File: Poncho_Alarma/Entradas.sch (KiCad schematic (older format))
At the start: 24 parts

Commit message: Esquematico Terminado
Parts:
- added J3: Entradas, symbol Connector_Generic:Conn_01x04
- U1: renamed from U?; symbol EESTN5:TLP627-4 -> Poncho_Alarma-rescue:TLP627-4-EESTN5
- gave numbers to parts that had none: 20
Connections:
- net GND: now also U1.11, U1.13, U1.4, U1.6, U1.8, U1.9; no longer U1.15, U1.15, U1.15, U1.2, U1.2, U1.2
- net at R11.2, R7.2: now also U1.3; no longer U1.1
- net at D6.1 (K), R17.2: now also U1.14, J3.1 (Pin_1); no longer U1.16
- net +3V3: now reaches R16.1, R17.1
- net +3V3: now also R14.1, R15.1, R18.1, R19.1, R20.1, R21.1
- net at R12.2, R8.2: now also U1.5; no longer U1.1
- net at D7.1 (K), R19.2: now also U1.12, J3.2 (Pin_2); no longer U1.16
- net at R13.2, R9.2: now also U1.7; no longer U1.1
- net at D8.1 (K), R21.2: now also U1.10, J3.3 (Pin_3); no longer U1.16
- net at D5.1 (K), R15.2, U1.16: now also J3.4 (Pin_4)
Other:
- moved on the sheet: D5, D8, R10, R13, R14, R15, R20, R21, R6, R9, U1A

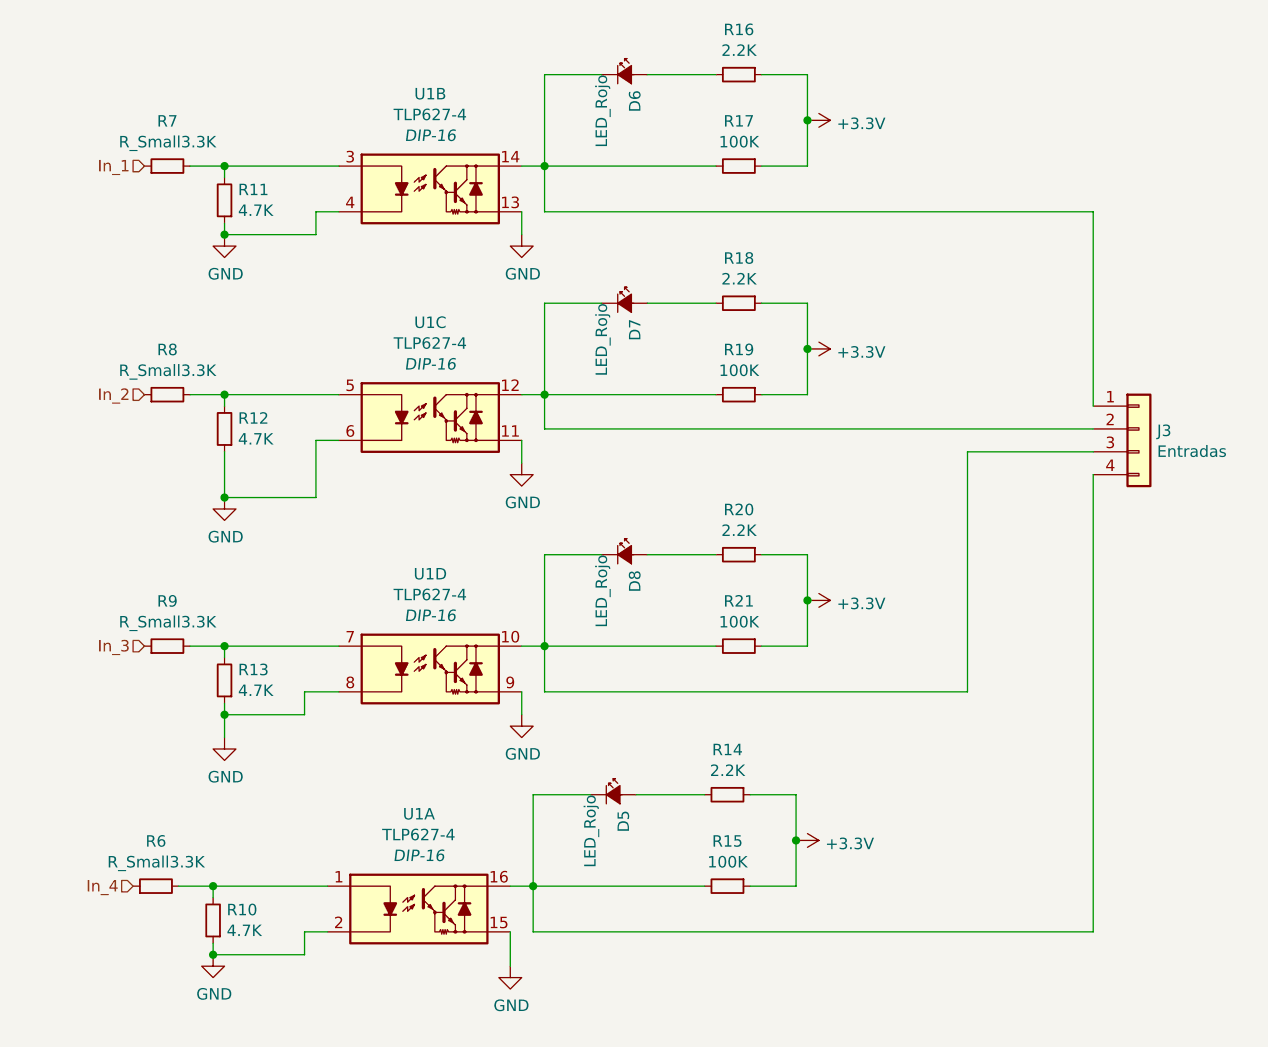
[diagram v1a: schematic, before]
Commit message: asociando componentes
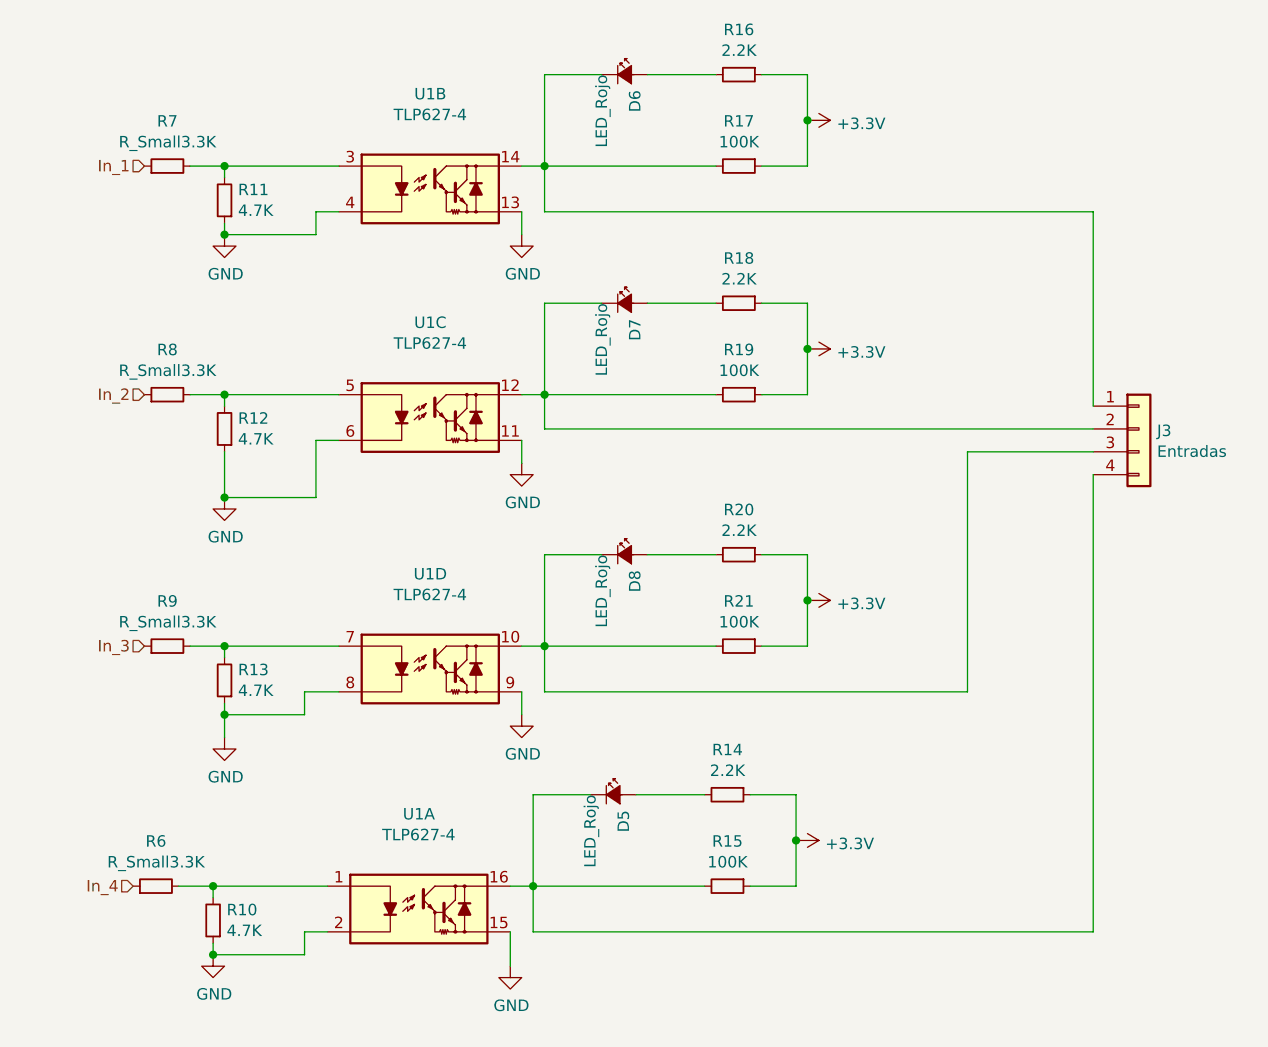
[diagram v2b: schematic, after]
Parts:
- D5, D6, D7, D8: footprint (none) -> LED_SMD:LED_0603_1608Metric_Pad1.05x0.95mm_HandSolder
- J3: footprint (none) -> TerminalBlock:TerminalBlock_bornier-4_P5.08mm
- R10, R11, R12, R13, R14, R15, R16, R17, R18, R19, R20, R21, R6, R7, R8, R9: footprint (none) -> Resistor_SMD:R_0603_1608Metric_Pad1.05x0.95mm_HandSolder
- U1: footprint DIP-16 -> Poncho-PLC:DIP_16-300_socket
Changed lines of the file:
@@
 F 0 "U1" H 4800 2515 50  0000 C CNN
 F 1 "TLP627-4" H 4800 2424 50  0000 C CNN
-F 2 "DIP-16" H 4800 2333 50  0000 C CIN
+F 2 "Poncho-PLC:DIP_16-300_socket" H 4800 2333 50  0001 C CIN
 F 3 "" H 4800 2100 50  0000 L CNN
 	2    4800 2100
@@
 F 0 "D6" V 5696 1532 50  0000 R CNN
 F 1 "LED_Rojo" V 5550 1600 50  0000 R CNN
-F 2 "" V 5650 1600 50  0001 C CNN
+F 2 "LED_SMD:LED_0603_1608Metric_Pad1.05x0.95mm_HandSolder" V 5650 1600 50  0001 C CNN
 F 3 "~" V 5650 1600 50  0001 C CNN
 	1    5650 1600
@@
 F 0 "R16" V 5954 1600 50  0000 C CNN
 F 1 "2.2K" V 6045 1600 50  0000 C CNN
-F 2 "" H 6150 1600 50  0001 C CNN
+F 2 "Resistor_SMD:R_0603_1608Metric_Pad1.05x0.95mm_HandSolder" H 6150 1600 50  0001 C CNN
 F 3 "~" H 6150 1600 50  0001 C CNN
 	1    6150 1600
@@
 F 0 "R17" V 5954 2000 50  0000 C CNN
 F 1 "100K" V 6045 2000 50  0000 C CNN
-F 2 "" H 6150 2000 50  0001 C CNN
+F 2 "Resistor_SMD:R_0603_1608Metric_Pad1.05x0.95mm_HandSolder" H 6150 2000 50  0001 C CNN
 F 3 "~" H 6150 2000 50  0001 C CNN
 	1    6150 2000
@@
 F 0 "R7" V 3846 2000 50  0000 C CNN
 F 1 "R_Small3.3K" V 3755 2000 50  0000 C CNN
-F 2 "" H 3650 2000 50  0001 C CNN
+F 2 "Resistor_SMD:R_0603_1608Metric_Pad1.05x0.95mm_HandSolder" H 3650 2000 50  0001 C CNN
 F 3 "~" H 3650 2000 50  0001 C CNN
 	1    3650 2000
@@
 F 0 "R11" H 3841 2104 50  0000 R CNN
 F 1 "4.7K" H 3841 2195 50  0000 R CNN
-F 2 "" H 3900 2150 50  0001 C CNN
+F 2 "Resistor_SMD:R_0603_1608Metric_Pad1.05x0.95mm_HandSolder" H 3900 2150 50  0001 C CNN
 F 3 "~" H 3900 2150 50  0001 C CNN
 	1    3900 2150
@@
 F 0 "U1" H 4800 3515 50  0000 C CNN
 F 1 "TLP627-4" H 4800 3424 50  0000 C CNN
-F 2 "DIP-16" H 4800 3333 50  0000 C CIN
+F 2 "Poncho-PLC:DIP_16-300_socket" H 4800 3333 50  0001 C CIN
 F 3 "" H 4800 3100 50  0000 L CNN
 	3    4800 3100
@@
 F 0 "D7" V 5696 2532 50  0000 R CNN
 F 1 "LED_Rojo" V 5550 2600 50  0000 R CNN
-F 2 "" V 5650 2600 50  0001 C CNN
+F 2 "LED_SMD:LED_0603_1608Metric_Pad1.05x0.95mm_HandSolder" V 5650 2600 50  0001 C CNN
 F 3 "~" V 5650 2600 50  0001 C CNN
 	1    5650 2600
@@
 F 0 "R18" V 5954 2600 50  0000 C CNN
 F 1 "2.2K" V 6045 2600 50  0000 C CNN
-F 2 "" H 6150 2600 50  0001 C CNN
+F 2 "Resistor_SMD:R_0603_1608Metric_Pad1.05x0.95mm_HandSolder" H 6150 2600 50  0001 C CNN
 F 3 "~" H 6150 2600 50  0001 C CNN
 	1    6150 2600
@@
 F 0 "R19" V 5954 3000 50  0000 C CNN
 F 1 "100K" V 6045 3000 50  0000 C CNN
-F 2 "" H 6150 3000 50  0001 C CNN
+F 2 "Resistor_SMD:R_0603_1608Metric_Pad1.05x0.95mm_HandSolder" H 6150 3000 50  0001 C CNN
 F 3 "~" H 6150 3000 50  0001 C CNN
 	1    6150 3000
@@
 F 0 "R8" V 3846 3000 50  0000 C CNN
 F 1 "R_Small3.3K" V 3755 3000 50  0000 C CNN
-F 2 "" H 3650 3000 50  0001 C CNN
+F 2 "Resistor_SMD:R_0603_1608Metric_Pad1.05x0.95mm_HandSolder" H 3650 3000 50  0001 C CNN
 F 3 "~" H 3650 3000 50  0001 C CNN
 	1    3650 3000
@@
 F 0 "R12" H 3841 3104 50  0000 R CNN
 F 1 "4.7K" H 3841 3195 50  0000 R CNN
-F 2 "" H 3900 3150 50  0001 C CNN
+F 2 "Resistor_SMD:R_0603_1608Metric_Pad1.05x0.95mm_HandSolder" H 3900 3150 50  0001 C CNN
 F 3 "~" H 3900 3150 50  0001 C CNN
 	1    3900 3150
@@
 F 0 "U1" H 4800 4615 50  0000 C CNN
 F 1 "TLP627-4" H 4800 4524 50  0000 C CNN
-F 2 "DIP-16" H 4800 4433 50  0000 C CIN
+F 2 "Poncho-PLC:DIP_16-300_socket" H 4800 4433 50  0001 C CIN
 F 3 "" H 4800 4200 50  0000 L CNN
 	4    4800 4200
@@
 F 0 "D8" V 5696 3632 50  0000 R CNN
 F 1 "LED_Rojo" V 5550 3700 50  0000 R CNN
-F 2 "" V 5650 3700 50  0001 C CNN
+F 2 "LED_SMD:LED_0603_1608Metric_Pad1.05x0.95mm_HandSolder" V 5650 3700 50  0001 C CNN
 F 3 "~" V 5650 3700 50  0001 C CNN
 	1    5650 3700
@@
 F 0 "R20" V 5954 3700 50  0000 C CNN
 F 1 "2.2K" V 6045 3700 50  0000 C CNN
-F 2 "" H 6150 3700 50  0001 C CNN
+F 2 "Resistor_SMD:R_0603_1608Metric_Pad1.05x0.95mm_HandSolder" H 6150 3700 50  0001 C CNN
 F 3 "~" H 6150 3700 50  0001 C CNN
 	1    6150 3700
@@
 F 0 "R21" V 5954 4100 50  0000 C CNN
 F 1 "100K" V 6045 4100 50  0000 C CNN
-F 2 "" H 6150 4100 50  0001 C CNN
+F 2 "Resistor_SMD:R_0603_1608Metric_Pad1.05x0.95mm_HandSolder" H 6150 4100 50  0001 C CNN
 F 3 "~" H 6150 4100 50  0001 C CNN
 	1    6150 4100
@@
 F 0 "R9" V 3846 4100 50  0000 C CNN
 F 1 "R_Small3.3K" V 3755 4100 50  0000 C CNN
-F 2 "" H 3650 4100 50  0001 C CNN
+F 2 "Resistor_SMD:R_0603_1608Metric_Pad1.05x0.95mm_HandSolder" H 3650 4100 50  0001 C CNN
 F 3 "~" H 3650 4100 50  0001 C CNN
 	1    3650 4100
@@
 F 0 "R13" H 3841 4204 50  0000 R CNN
 F 1 "4.7K" H 3841 4295 50  0000 R CNN
-F 2 "" H 3900 4250 50  0001 C CNN
+F 2 "Resistor_SMD:R_0603_1608Metric_Pad1.05x0.95mm_HandSolder" H 3900 4250 50  0001 C CNN
 F 3 "~" H 3900 4250 50  0001 C CNN
 	1    3900 4250
@@
 F 0 "U1" H 4750 5665 50  0000 C CNN
 F 1 "TLP627-4" H 4750 5574 50  0000 C CNN
-F 2 "DIP-16" H 4750 5483 50  0000 C CIN
+F 2 "Poncho-PLC:DIP_16-300_socket" H 4750 5483 50  0001 C CIN
 F 3 "" H 4750 5250 50  0000 L CNN
 	1    4750 5250
@@
 F 0 "D5" V 5646 4682 50  0000 R CNN
 F 1 "LED_Rojo" V 5500 4750 50  0000 R CNN
-F 2 "" V 5600 4750 50  0001 C CNN
+F 2 "LED_SMD:LED_0603_1608Metric_Pad1.05x0.95mm_HandSolder" V 5600 4750 50  0001 C CNN
 F 3 "~" V 5600 4750 50  0001 C CNN
 	1    5600 4750
@@
 F 0 "R14" V 5904 4750 50  0000 C CNN
 F 1 "2.2K" V 5995 4750 50  0000 C CNN
-F 2 "" H 6100 4750 50  0001 C CNN
+F 2 "Resistor_SMD:R_0603_1608Metric_Pad1.05x0.95mm_HandSolder" H 6100 4750 50  0001 C CNN
 F 3 "~" H 6100 4750 50  0001 C CNN
 	1    6100 4750
@@
 F 0 "R15" V 5904 5150 50  0000 C CNN
 F 1 "100K" V 5995 5150 50  0000 C CNN
-F 2 "" H 6100 5150 50  0001 C CNN
+F 2 "Resistor_SMD:R_0603_1608Metric_Pad1.05x0.95mm_HandSolder" H 6100 5150 50  0001 C CNN
 F 3 "~" H 6100 5150 50  0001 C CNN
 	1    6100 5150
@@
 F 0 "R6" V 3796 5150 50  0000 C CNN
 F 1 "R_Small3.3K" V 3705 5150 50  0000 C CNN
-F 2 "" H 3600 5150 50  0001 C CNN
+F 2 "Resistor_SMD:R_0603_1608Metric_Pad1.05x0.95mm_HandSolder" H 3600 5150 50  0001 C CNN
 F 3 "~" H 3600 5150 50  0001 C CNN
 	1    3600 5150
@@
 F 0 "R10" H 3791 5254 50  0000 R CNN
 F 1 "4.7K" H 3791 5345 50  0000 R CNN
-F 2 "" H 3850 5300 50  0001 C CNN
+F 2 "Resistor_SMD:R_0603_1608Metric_Pad1.05x0.95mm_HandSolder" H 3850 5300 50  0001 C CNN
 F 3 "~" H 3850 5300 50  0001 C CNN
 	1    3850 5300
@@
 F 0 "J3" H 7979 3142 50  0000 L CNN
 F 1 "Entradas" H 7979 3051 50  0000 L CNN
-F 2 "" H 7900 3150 50  0001 C CNN
+F 2 "TerminalBlock:TerminalBlock_bornier-4_P5.08mm" H 7900 3150 50  0001 C CNN
 F 3 "~" H 7900 3150 50  0001 C CNN
 	1    7900 3150

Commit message: arreglado lo de la libreria
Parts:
- D5, D6, D7, D8: footprint LED_SMD:LED_0603_1608Metric_Pad1.05x0.95mm_HandSolder -> LED_THT:LED_D3.0mm
- R10, R11, R12, R13, R14, R15, R16, R17, R18, R19, R20, R21, R6, R7, R8, R9: footprint Resistor_SMD:R_0603_1608Metric_Pad1.05x0.95mm_HandSolder -> Resistor_THT:R_Axial_DIN0204_L3.6mm_D1.6mm_P5.08mm_Horizontal
- U1: footprint Poncho-PLC:DIP_16-300_socket -> Package_DIP:DIP-16_W7.62mm
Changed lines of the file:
@@
 F 0 "U1" H 4800 2515 50  0000 C CNN
 F 1 "TLP627-4" H 4800 2424 50  0000 C CNN
-F 2 "Poncho-PLC:DIP_16-300_socket" H 4800 2333 50  0001 C CIN
+F 2 "Package_DIP:DIP-16_W7.62mm" H 4800 2333 50  0001 C CIN
 F 3 "" H 4800 2100 50  0000 L CNN
 	2    4800 2100
@@
 F 0 "D6" V 5696 1532 50  0000 R CNN
 F 1 "LED_Rojo" V 5550 1600 50  0000 R CNN
-F 2 "LED_SMD:LED_0603_1608Metric_Pad1.05x0.95mm_HandSolder" V 5650 1600 50  0001 C CNN
+F 2 "LED_THT:LED_D3.0mm" V 5650 1600 50  0001 C CNN
 F 3 "~" V 5650 1600 50  0001 C CNN
 	1    5650 1600
@@
 F 0 "R16" V 5954 1600 50  0000 C CNN
 F 1 "2.2K" V 6045 1600 50  0000 C CNN
-F 2 "Resistor_SMD:R_0603_1608Metric_Pad1.05x0.95mm_HandSolder" H 6150 1600 50  0001 C CNN
+F 2 "Resistor_THT:R_Axial_DIN0204_L3.6mm_D1.6mm_P5.08mm_Horizontal" H 6150 1600 50  0001 C CNN
 F 3 "~" H 6150 1600 50  0001 C CNN
 	1    6150 1600
@@
 F 0 "R17" V 5954 2000 50  0000 C CNN
 F 1 "100K" V 6045 2000 50  0000 C CNN
-F 2 "Resistor_SMD:R_0603_1608Metric_Pad1.05x0.95mm_HandSolder" H 6150 2000 50  0001 C CNN
+F 2 "Resistor_THT:R_Axial_DIN0204_L3.6mm_D1.6mm_P5.08mm_Horizontal" H 6150 2000 50  0001 C CNN
 F 3 "~" H 6150 2000 50  0001 C CNN
 	1    6150 2000
@@
 F 0 "R7" V 3846 2000 50  0000 C CNN
 F 1 "R_Small3.3K" V 3755 2000 50  0000 C CNN
-F 2 "Resistor_SMD:R_0603_1608Metric_Pad1.05x0.95mm_HandSolder" H 3650 2000 50  0001 C CNN
+F 2 "Resistor_THT:R_Axial_DIN0204_L3.6mm_D1.6mm_P5.08mm_Horizontal" H 3650 2000 50  0001 C CNN
 F 3 "~" H 3650 2000 50  0001 C CNN
 	1    3650 2000
@@
 F 0 "R11" H 3841 2104 50  0000 R CNN
 F 1 "4.7K" H 3841 2195 50  0000 R CNN
-F 2 "Resistor_SMD:R_0603_1608Metric_Pad1.05x0.95mm_HandSolder" H 3900 2150 50  0001 C CNN
+F 2 "Resistor_THT:R_Axial_DIN0204_L3.6mm_D1.6mm_P5.08mm_Horizontal" H 3900 2150 50  0001 C CNN
 F 3 "~" H 3900 2150 50  0001 C CNN
 	1    3900 2150
@@
 F 0 "U1" H 4800 3515 50  0000 C CNN
 F 1 "TLP627-4" H 4800 3424 50  0000 C CNN
-F 2 "Poncho-PLC:DIP_16-300_socket" H 4800 3333 50  0001 C CIN
+F 2 "Package_DIP:DIP-16_W7.62mm" H 4800 3333 50  0001 C CIN
 F 3 "" H 4800 3100 50  0000 L CNN
 	3    4800 3100
@@
 F 0 "D7" V 5696 2532 50  0000 R CNN
 F 1 "LED_Rojo" V 5550 2600 50  0000 R CNN
-F 2 "LED_SMD:LED_0603_1608Metric_Pad1.05x0.95mm_HandSolder" V 5650 2600 50  0001 C CNN
+F 2 "LED_THT:LED_D3.0mm" V 5650 2600 50  0001 C CNN
 F 3 "~" V 5650 2600 50  0001 C CNN
 	1    5650 2600
@@
 F 0 "R18" V 5954 2600 50  0000 C CNN
 F 1 "2.2K" V 6045 2600 50  0000 C CNN
-F 2 "Resistor_SMD:R_0603_1608Metric_Pad1.05x0.95mm_HandSolder" H 6150 2600 50  0001 C CNN
+F 2 "Resistor_THT:R_Axial_DIN0204_L3.6mm_D1.6mm_P5.08mm_Horizontal" H 6150 2600 50  0001 C CNN
 F 3 "~" H 6150 2600 50  0001 C CNN
 	1    6150 2600
@@
 F 0 "R19" V 5954 3000 50  0000 C CNN
 F 1 "100K" V 6045 3000 50  0000 C CNN
-F 2 "Resistor_SMD:R_0603_1608Metric_Pad1.05x0.95mm_HandSolder" H 6150 3000 50  0001 C CNN
+F 2 "Resistor_THT:R_Axial_DIN0204_L3.6mm_D1.6mm_P5.08mm_Horizontal" H 6150 3000 50  0001 C CNN
 F 3 "~" H 6150 3000 50  0001 C CNN
 	1    6150 3000
@@
 F 0 "R8" V 3846 3000 50  0000 C CNN
 F 1 "R_Small3.3K" V 3755 3000 50  0000 C CNN
-F 2 "Resistor_SMD:R_0603_1608Metric_Pad1.05x0.95mm_HandSolder" H 3650 3000 50  0001 C CNN
+F 2 "Resistor_THT:R_Axial_DIN0204_L3.6mm_D1.6mm_P5.08mm_Horizontal" H 3650 3000 50  0001 C CNN
 F 3 "~" H 3650 3000 50  0001 C CNN
 	1    3650 3000
@@
 F 0 "R12" H 3841 3104 50  0000 R CNN
 F 1 "4.7K" H 3841 3195 50  0000 R CNN
-F 2 "Resistor_SMD:R_0603_1608Metric_Pad1.05x0.95mm_HandSolder" H 3900 3150 50  0001 C CNN
+F 2 "Resistor_THT:R_Axial_DIN0204_L3.6mm_D1.6mm_P5.08mm_Horizontal" H 3900 3150 50  0001 C CNN
 F 3 "~" H 3900 3150 50  0001 C CNN
 	1    3900 3150
@@
 F 0 "U1" H 4800 4615 50  0000 C CNN
 F 1 "TLP627-4" H 4800 4524 50  0000 C CNN
-F 2 "Poncho-PLC:DIP_16-300_socket" H 4800 4433 50  0001 C CIN
+F 2 "Package_DIP:DIP-16_W7.62mm" H 4800 4433 50  0001 C CIN
 F 3 "" H 4800 4200 50  0000 L CNN
 	4    4800 4200
@@
 F 0 "D8" V 5696 3632 50  0000 R CNN
 F 1 "LED_Rojo" V 5550 3700 50  0000 R CNN
-F 2 "LED_SMD:LED_0603_1608Metric_Pad1.05x0.95mm_HandSolder" V 5650 3700 50  0001 C CNN
+F 2 "LED_THT:LED_D3.0mm" V 5650 3700 50  0001 C CNN
 F 3 "~" V 5650 3700 50  0001 C CNN
 	1    5650 3700
@@
 F 0 "R20" V 5954 3700 50  0000 C CNN
 F 1 "2.2K" V 6045 3700 50  0000 C CNN
-F 2 "Resistor_SMD:R_0603_1608Metric_Pad1.05x0.95mm_HandSolder" H 6150 3700 50  0001 C CNN
+F 2 "Resistor_THT:R_Axial_DIN0204_L3.6mm_D1.6mm_P5.08mm_Horizontal" H 6150 3700 50  0001 C CNN
 F 3 "~" H 6150 3700 50  0001 C CNN
 	1    6150 3700
@@
 F 0 "R21" V 5954 4100 50  0000 C CNN
 F 1 "100K" V 6045 4100 50  0000 C CNN
-F 2 "Resistor_SMD:R_0603_1608Metric_Pad1.05x0.95mm_HandSolder" H 6150 4100 50  0001 C CNN
+F 2 "Resistor_THT:R_Axial_DIN0204_L3.6mm_D1.6mm_P5.08mm_Horizontal" H 6150 4100 50  0001 C CNN
 F 3 "~" H 6150 4100 50  0001 C CNN
 	1    6150 4100
@@
 F 0 "R9" V 3846 4100 50  0000 C CNN
 F 1 "R_Small3.3K" V 3755 4100 50  0000 C CNN
-F 2 "Resistor_SMD:R_0603_1608Metric_Pad1.05x0.95mm_HandSolder" H 3650 4100 50  0001 C CNN
+F 2 "Resistor_THT:R_Axial_DIN0204_L3.6mm_D1.6mm_P5.08mm_Horizontal" H 3650 4100 50  0001 C CNN
 F 3 "~" H 3650 4100 50  0001 C CNN
 	1    3650 4100
@@
 F 0 "R13" H 3841 4204 50  0000 R CNN
 F 1 "4.7K" H 3841 4295 50  0000 R CNN
-F 2 "Resistor_SMD:R_0603_1608Metric_Pad1.05x0.95mm_HandSolder" H 3900 4250 50  0001 C CNN
+F 2 "Resistor_THT:R_Axial_DIN0204_L3.6mm_D1.6mm_P5.08mm_Horizontal" H 3900 4250 50  0001 C CNN
 F 3 "~" H 3900 4250 50  0001 C CNN
 	1    3900 4250
@@
 F 0 "U1" H 4750 5665 50  0000 C CNN
 F 1 "TLP627-4" H 4750 5574 50  0000 C CNN
-F 2 "Poncho-PLC:DIP_16-300_socket" H 4750 5483 50  0001 C CIN
+F 2 "Package_DIP:DIP-16_W7.62mm" H 4750 5483 50  0001 C CIN
 F 3 "" H 4750 5250 50  0000 L CNN
 	1    4750 5250
@@
 F 0 "D5" V 5646 4682 50  0000 R CNN
 F 1 "LED_Rojo" V 5500 4750 50  0000 R CNN
-F 2 "LED_SMD:LED_0603_1608Metric_Pad1.05x0.95mm_HandSolder" V 5600 4750 50  0001 C CNN
+F 2 "LED_THT:LED_D3.0mm" V 5600 4750 50  0001 C CNN
 F 3 "~" V 5600 4750 50  0001 C CNN
 	1    5600 4750
@@
 F 0 "R14" V 5904 4750 50  0000 C CNN
 F 1 "2.2K" V 5995 4750 50  0000 C CNN
-F 2 "Resistor_SMD:R_0603_1608Metric_Pad1.05x0.95mm_HandSolder" H 6100 4750 50  0001 C CNN
+F 2 "Resistor_THT:R_Axial_DIN0204_L3.6mm_D1.6mm_P5.08mm_Horizontal" H 6100 4750 50  0001 C CNN
 F 3 "~" H 6100 4750 50  0001 C CNN
 	1    6100 4750
@@
 F 0 "R15" V 5904 5150 50  0000 C CNN
 F 1 "100K" V 5995 5150 50  0000 C CNN
-F 2 "Resistor_SMD:R_0603_1608Metric_Pad1.05x0.95mm_HandSolder" H 6100 5150 50  0001 C CNN
+F 2 "Resistor_THT:R_Axial_DIN0204_L3.6mm_D1.6mm_P5.08mm_Horizontal" H 6100 5150 50  0001 C CNN
 F 3 "~" H 6100 5150 50  0001 C CNN
 	1    6100 5150
@@
 F 0 "R6" V 3796 5150 50  0000 C CNN
 F 1 "R_Small3.3K" V 3705 5150 50  0000 C CNN
-F 2 "Resistor_SMD:R_0603_1608Metric_Pad1.05x0.95mm_HandSolder" H 3600 5150 50  0001 C CNN
+F 2 "Resistor_THT:R_Axial_DIN0204_L3.6mm_D1.6mm_P5.08mm_Horizontal" H 3600 5150 50  0001 C CNN
 F 3 "~" H 3600 5150 50  0001 C CNN
 	1    3600 5150
@@
 F 0 "R10" H 3791 5254 50  0000 R CNN
 F 1 "4.7K" H 3791 5345 50  0000 R CNN
-F 2 "Resistor_SMD:R_0603_1608Metric_Pad1.05x0.95mm_HandSolder" H 3850 5300 50  0001 C CNN
+F 2 "Resistor_THT:R_Axial_DIN0204_L3.6mm_D1.6mm_P5.08mm_Horizontal" H 3850 5300 50  0001 C CNN
 F 3 "~" H 3850 5300 50  0001 C CNN
 	1    3850 5300
